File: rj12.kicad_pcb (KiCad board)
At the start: 2 copper layers, 16.3 x 21 mm, 2 parts, among them J1 Conn_01x06, P1 RJ12_Housing

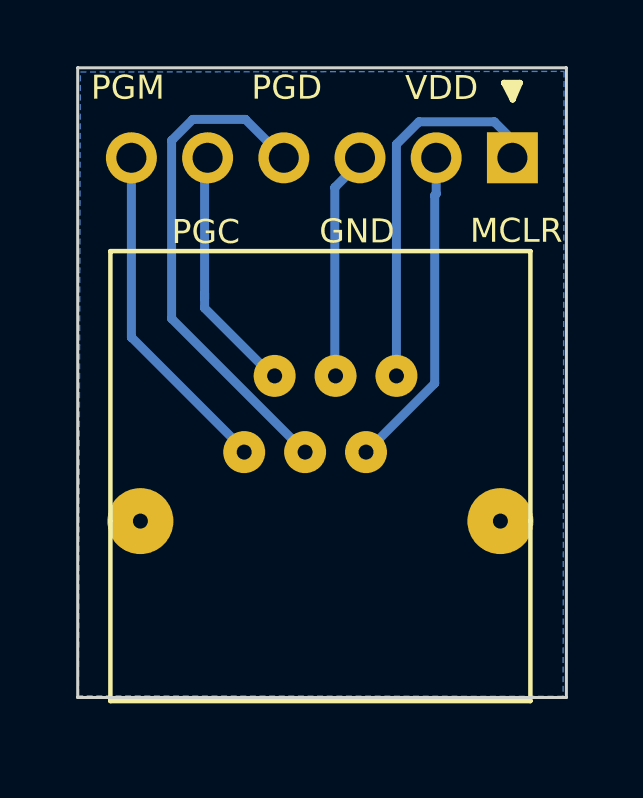
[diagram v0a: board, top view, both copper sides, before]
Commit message: Copper-Poured with Pin3 and placed the indicator closer to the pin
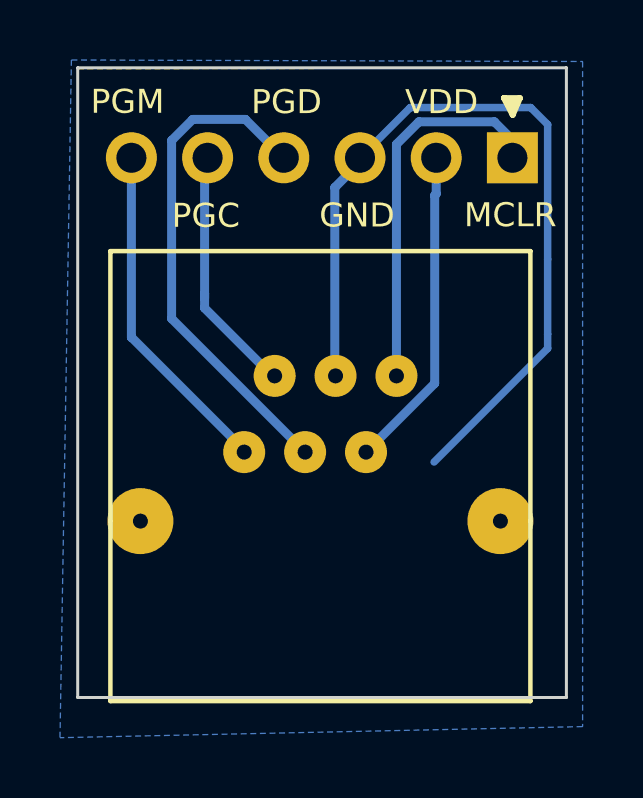
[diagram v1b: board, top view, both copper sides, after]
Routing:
- net pin3: track 7.76 -> 27.8 mm
- added copper zone on B.Cu, net pin3
- added copper zone on F.Cu, net pin3
- removed copper zone on B.Cu, net (none)
- removed copper zone on F.Cu, net (none)
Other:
- board text added: "ICD3_Conn"
- board text removed: "ICD3 Conn"
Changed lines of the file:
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@@
     (thickness 1.6)
     (drawings 31)
-    (tracks 29)
+    (tracks 36)
     (zones 0)
     (modules 2)
@@
     )
   )
-  (gr_line (start 174.14 100) (end 173.9 100.56) (layer F.SilkS) (width 0.2))
-  (gr_line (start 173.61 100) (end 174.14 100) (layer F.SilkS) (width 0.2))
+  (gr_line (start 174.14 100.51) (end 173.9 101.07) (layer F.SilkS) (width 0.2))
+  (gr_line (start 173.61 100.51) (end 174.14 100.51) (layer F.SilkS) (width 0.2))
   (gr_line (start 175.69 99.5) (end 175.69 120.49) (layer Edge.Cuts) (width 0.1))
   (gr_line (start 166.59 116.81) (end 165.91 117.33) (layer B.SilkS) (width 0.2))
@@
   (gr_line (start 168.18 114.75) (end 168.88 114.26) (layer B.SilkS) (width 0.2))
   (gr_circle (center 167.573887 116.12) (end 168.443887 114.99) (layer B.SilkS) (width 0.2))
-  (gr_line (start 173.95 100.16) (end 173.9 100.25) (layer F.SilkS) (width 0.2))
-  (gr_line (start 173.61 100) (end 173.95 100.16) (layer F.SilkS) (width 0.2))
-  (gr_line (start 173.9 100.56) (end 173.61 100) (layer F.SilkS) (width 0.2))
-  (gr_text "ICD3 Conn" (at 167.6 118.77) (layer B.SilkS)
+  (gr_line (start 173.95 100.67) (end 173.9 100.76) (layer F.SilkS) (width 0.2))
+  (gr_line (start 173.61 100.51) (end 173.95 100.67) (layer F.SilkS) (width 0.2))
+  (gr_line (start 173.9 101.07) (end 173.61 100.51) (layer F.SilkS) (width 0.2))
+  (gr_text ICD3_Conn (at 167.6 118.77) (layer B.SilkS)
     (effects (font (size 1 1) (thickness 0.25)) (justify mirror))
   )
@@
   (gr_line (start 159.4 99.5) (end 175.69 99.5) (layer Edge.Cuts) (width 0.1))
   (gr_line (start 159.4 120.49) (end 175.69 120.49) (layer Edge.Cuts) (width 0.1))
-  (gr_text PGM (at 161.07 100.16) (layer F.SilkS)
-    (effects (font (size 0.8 0.8) (thickness 0.2)))
-  )
-  (gr_text PGC (at 163.67 104.97) (layer F.SilkS)
-    (effects (font (size 0.8 0.8) (thickness 0.2)))
-  )
-  (gr_text PGD (at 166.37 100.16) (layer F.SilkS)
-    (effects (font (size 0.8 0.8) (thickness 0.2)))
-  )
-  (gr_text GND (at 168.71 104.95) (layer F.SilkS)
-    (effects (font (size 0.8 0.8) (thickness 0.2)))
-  )
-  (gr_text VDD (at 171.53 100.17) (layer F.SilkS)
-    (effects (font (size 0.8 0.8) (thickness 0.2)))
-  )
-  (gr_text MCLR (at 174.02 104.93) (layer F.SilkS)
+  (gr_text PGM (at 161.06 100.63) (layer F.SilkS)
+    (effects (font (size 0.8 0.8) (thickness 0.2)))
+  )
+  (gr_text PGC (at 163.67 104.43) (layer F.SilkS)
+    (effects (font (size 0.8 0.8) (thickness 0.2)))
+  )
+  (gr_text PGD (at 166.36 100.64) (layer F.SilkS)
+    (effects (font (size 0.8 0.8) (thickness 0.2)))
+  )
+  (gr_text GND (at 168.71 104.42) (layer F.SilkS)
+    (effects (font (size 0.8 0.8) (thickness 0.2)))
+  )
+  (gr_text VDD (at 171.53 100.64) (layer F.SilkS)
+    (effects (font (size 0.8 0.8) (thickness 0.2)))
+  )
+  (gr_text MCLR (at 173.82 104.41) (layer F.SilkS)
     (effects (font (size 0.8 0.8) (thickness 0.2)))
   )
@@
   (segment (start 171.5 102.5) (end 171.3 102.7) (width 0.3) (layer B.Cu) (net 2))
   (segment (start 171.3 110.02) (end 169.01 112.31) (width 0.3) (layer B.Cu) (net 2))
+  (segment (start 175.065001 108.854999) (end 171.28 112.64) (width 0.25) (layer B.Cu) (net 3))
+  (segment (start 175.065001 108.374999) (end 175.065001 108.854999) (width 0.25) (layer B.Cu) (net 3))
+  (segment (start 175.065001 105.884999) (end 175.065001 108.374999) (width 0.25) (layer B.Cu) (net 3))
+  (segment (start 168.81 102.5) (end 170.485011 100.824989) (width 0.25) (layer B.Cu) (net 3))
+  (segment (start 170.485011 100.824989) (end 174.499991 100.824989) (width 0.25) (layer B.Cu) (net 3))
+  (segment (start 174.499991 100.824989) (end 175.065001 101.389999) (width 0.25) (layer B.Cu) (net 3))
+  (segment (start 175.065001 101.389999) (end 175.065001 105.884999) (width 0.25) (layer B.Cu) (net 3))
   (segment (start 168.96 102.5) (end 167.970005 103.489995) (width 0.3) (layer B.Cu) (net 3))
   (segment (start 167.970005 103.489995) (end 167.970005 109.745005) (width 0.3) (layer B.Cu) (net 3))
@@
   (segment (start 161.195 108.485) (end 164.95 112.24) (width 0.3) (layer B.Cu) (net 6))
   (segment (start 161.34 102.5) (end 161.16 102.68) (width 0.3) (layer B.Cu) (net 6))
-  (zone (net 0) (net_name "") (layer F.Cu) (hatch edge 0.508)
+  (zone (net 3) (net_name pin3) (layer F.Cu) (hatch edge 0.508)
     (connect_pads (clearance 0.508))
     (min_thickness 0.254)
@@
     (polygon
       (pts
-        (xy 159.4 99.5) (xy 175.69 99.51) (xy 175.7 120.49) (xy 159.4 120.46)
+        (xy 159.4 99.54) (xy 175.7 99.5) (xy 175.69 120.5) (xy 159.4 120.49)
       )
     )
   )
-  (zone (net 0) (net_name "") (layer B.Cu) (hatch edge 0.508)
+  (zone (net 3) (net_name pin3) (layer B.Cu) (hatch edge 0.508)
     (connect_pads (clearance 0.508))
     (min_thickness 0.254)
@@
     (polygon
       (pts
-        (xy 159.49 99.64) (xy 175.61 99.62) (xy 175.58 120.45) (xy 159.43 120.43)
+        (xy 159.19 99.24) (xy 176.23 99.29) (xy 176.23 121.46) (xy 158.81 121.83)
       )
     )
